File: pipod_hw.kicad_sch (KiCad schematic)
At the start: 0 parts

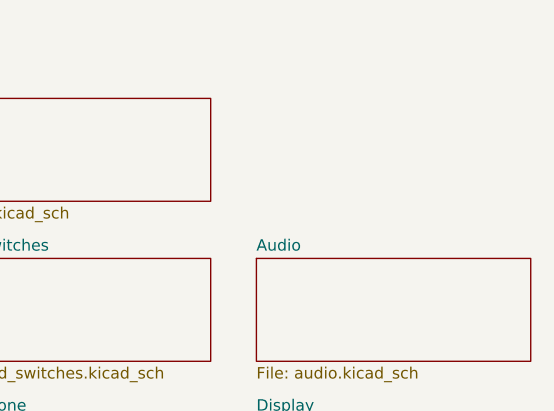
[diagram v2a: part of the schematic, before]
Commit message: integration: add mounting holes and connectors and second board
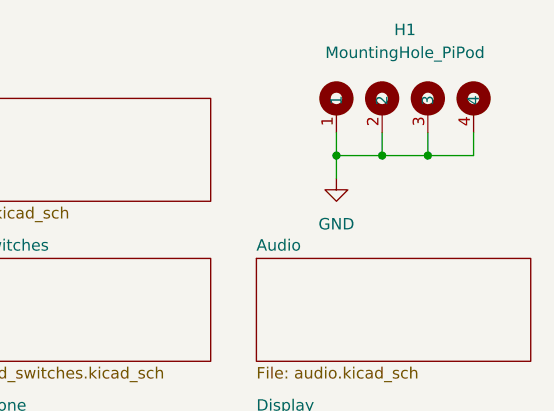
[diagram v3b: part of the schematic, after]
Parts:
- added H1: MountingHole_PiPod, pipod_hw:MountingHole_PiPod, symbol pipod_hw:MountingHole_PiPod
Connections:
- new net GND: H1.1, H1.2, H1.3, H1.4
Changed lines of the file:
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@@
 (kicad_sch (version 20211123) (generator eeschema)
   (paper "A4")
+  (junction (at 243.84 67.31) (diameter 0) (color 0 0 0 0)
+  )
+  (junction (at 233.68 67.31) (diameter 0) (color 0 0 0 0)
+  )
+  (junction (at 238.76 67.31) (diameter 0) (color 0 0 0 0)
+  )
+  (wire (pts (xy 238.76 67.31) (xy 233.68 67.31))
+    (stroke (width 0) (type default) (color 0 0 0 0))
+  )
+  (wire (pts (xy 233.68 64.77) (xy 233.68 67.31))
+    (stroke (width 0) (type default) (color 0 0 0 0))
+  )
+  (wire (pts (xy 248.92 64.77) (xy 248.92 67.31))
+    (stroke (width 0) (type default) (color 0 0 0 0))
+  )
+  (wire (pts (xy 243.84 64.77) (xy 243.84 67.31))
+    (stroke (width 0) (type default) (color 0 0 0 0))
+  )
+  (wire (pts (xy 243.84 67.31) (xy 238.76 67.31))
+    (stroke (width 0) (type default) (color 0 0 0 0))
+  )
+  (wire (pts (xy 233.68 67.31) (xy 233.68 69.85))
+    (stroke (width 0) (type default) (color 0 0 0 0))
+  )
+  (wire (pts (xy 248.92 67.31) (xy 243.84 67.31))
+    (stroke (width 0) (type default) (color 0 0 0 0))
+  )
+  (wire (pts (xy 238.76 64.77) (xy 238.76 67.31))
+    (stroke (width 0) (type default) (color 0 0 0 0))
+  )
+  (symbol (lib_id "pipod_hw:MountingHole_PiPod") (at 241.3 57.15 0) (unit 1)
+    (in_bom yes) (on_board yes) (fields_autoplaced)
+    (property "Reference" "H1" (id 0) (at 241.3 53.34 0))
+    (property "Value" "MountingHole_PiPod" (id 1) (at 241.3 55.88 0))
+    (property "Footprint" "pipod_hw:MountingHole_PiPod" (id 2) (at 241.3 57.15 0)
+      (effects (font (size 1.27 1.27)) hide)
+    )
+    (property "Datasheet" "" (id 3) (at 241.3 57.15 0)
+      (effects (font (size 1.27 1.27)) hide)
+    )
+    (pin "1")
+    (pin "2")
+    (pin "3")
+    (pin "4")
+  )
+  (symbol (lib_id "power:GND") (at 233.68 69.85 0) (unit 1)
+    (in_bom yes) (on_board yes) (fields_autoplaced)
+    (property "Reference" "#PWR0128" (id 0) (at 233.68 76.2 0)
+      (effects (font (size 1.27 1.27)) hide)
+    )
+    (property "Value" "GND" (id 1) (at 233.68 74.93 0))
+    (property "Footprint" "" (id 2) (at 233.68 69.85 0)
+      (effects (font (size 1.27 1.27)) hide)
+    )
+    (property "Datasheet" "" (id 3) (at 233.68 69.85 0)
+      (effects (font (size 1.27 1.27)) hide)
+    )
+    (pin "1")
+  )
   (sheet (at 189.23 78.74) (size 30.48 11.43) (fields_autoplaced)
     (stroke (width 0.1524) (type solid) (color 0 0 0 0))
@@
       (reference "#PWR0110") (unit 1) (value "GND") (footprint "")
     )
-    (path "/b0bb8e22-3ad5-4c36-b10d-7d4a51e22334/5f1a81a0-71fa-4e3a-b666-a1214c182b88"
+    (path "/b0bb8e22-3ad5-4c36-b10d-7d4a51e22334/c5850e11-500c-4afe-a940-57198437c49b"
       (reference "#PWR0111") (unit 1) (value "GND") (footprint "")
     )
@@
       (reference "#PWR0112") (unit 1) (value "GND") (footprint "")
     )
-    (path "/b0bb8e22-3ad5-4c36-b10d-7d4a51e22334/c9a079a4-a909-4c56-8f16-71ef57f1a02b"
+    (path "/b0bb8e22-3ad5-4c36-b10d-7d4a51e22334/92d3ff33-a56f-47b9-a155-1bb3f2f205ba"
       (reference "#PWR0113") (unit 1) (value "GND") (footprint "")
     )
-    (path "/b0bb8e22-3ad5-4c36-b10d-7d4a51e22334/7c31225e-d0aa-4e44-9f35-ab169480b0ab"
+    (path "/b0bb8e22-3ad5-4c36-b10d-7d4a51e22334/cc6524eb-94f3-4dfa-bdaa-99b0ca25d5ec"
       (reference "#PWR0114") (unit 1) (value "GND") (footprint "")
-    )
-    (path "/b0bb8e22-3ad5-4c36-b10d-7d4a51e22334/75ae250c-0f71-4135-b694-211ea9e1b346"
-      (reference "#PWR0115") (unit 1) (value "GND") (footprint "")
-    )
-    (path "/b0bb8e22-3ad5-4c36-b10d-7d4a51e22334/3afe4e73-fffb-46f1-9e1b-36443c4e46f7"
-      (reference "#PWR0116") (unit 1) (value "GND") (footprint "")
-    )
-    (path "/b0bb8e22-3ad5-4c36-b10d-7d4a51e22334/03da5625-23ea-48a9-8d0e-93afc8231c75"
-      (reference "#PWR0117") (unit 1) (value "GND") (footprint "")
-    )
-    (path "/b0bb8e22-3ad5-4c36-b10d-7d4a51e22334/c7b7372b-e3fe-413d-9bae-152c09962a64"
-      (reference "#PWR0118") (unit 1) (value "GND") (footprint "")
     )
     (path "/b0bb8e22-3ad5-4c36-b10d-7d4a51e22334/1187d984-3ec5-4c88-9c0f-ce193ae40d3e"
@@
       (reference "#PWR0127") (unit 1) (value "GNDA") (footprint "")
     )
+    (path "/c269cfd8-5b8f-4de0-b20e-7c84acf71936"
+      (reference "#PWR0128") (unit 1) (value "GND") (footprint "")
+    )
     (path "/9641055c-ce4b-4f2f-881f-d2622ca62ef8/69434326-4e70-4b27-bc99-d48bcdec69df"
       (reference "C1") (unit 1) (value "100n") (footprint "Capacitor_SMD:C_0402_1005Metric")
@@
       (reference "C53") (unit 1) (value "10u") (footprint "Capacitor_SMD:C_0402_1005Metric")
     )
-    (path "/b0bb8e22-3ad5-4c36-b10d-7d4a51e22334/dc70e79b-aa01-498d-83ce-04f8beba6a37"
-      (reference "CN1") (unit 1) (value "539160208") (footprint "lcsc:CONN-SMD_539160208")
-    )
-    (path "/b0bb8e22-3ad5-4c36-b10d-7d4a51e22334/d0e61b23-0984-4efd-a60c-569879ae3557"
-      (reference "CN2") (unit 1) (value "539160208") (footprint "lcsc:CONN-SMD_539160208")
-    )
     (path "/9641055c-ce4b-4f2f-881f-d2622ca62ef8/11a9f816-3064-4feb-beef-6cd42a49141b"
       (reference "D1") (unit 1) (value "MBRS130LT3G") (footprint "lcsc:SMB_L4.6-W3.6-LS5.3-RD")
@@
       (reference "DISP1") (unit 1) (value "STP240320_0200B") (footprint "Connector_Molex:Molex_SlimStack_54722-0164_2x08_P0.50mm_Vertical")
     )
+    (path "/b0bb8e22-3ad5-4c36-b10d-7d4a51e22334/3011643e-d10a-4918-abfd-3d280f17eb2f"
+      (reference "FPC1") (unit 1) (value "527462033") (footprint "lcsc:FPC-SMD_527462033")
+    )
+    (path "/b0bb8e22-3ad5-4c36-b10d-7d4a51e22334/3e4fc367-8c2e-4085-a0b0-e86f20d2a052"
+      (reference "FPC2") (unit 1) (value "527462033") (footprint "lcsc:FPC-SMD_527462033")
+    )
+    (path "/3a54314d-f300-4b26-9d74-86b079b327e3"
+      (reference "H1") (unit 1) (value "MountingHole_PiPod") (footprint "pipod_hw:MountingHole_PiPod")
+    )
     (path "/9641055c-ce4b-4f2f-881f-d2622ca62ef8/17c02880-df6f-4797-b976-af8c3295fb23"
       (reference "J3") (unit 1) (value "Conn_01x03_Male") (footprint "Gigahawk:Molex_PicoBlade_53047-0310_1x03_P1.25mm_Vertical")
@@
     )
     (path "/eadbe3e2-ad3f-4ca7-9baa-62c6cdfbb2dc/da0dae29-42d4-483a-9ab1-6e5fb7494f0a"
-      (reference "R12") (unit 1) (value "DNI") (footprint "")
+      (reference "R12") (unit 1) (value "DNI") (footprint "Resistor_SMD:R_0402_1005Metric")
     )
     (path "/f4aab422-c542-43e3-8476-eae6a2df1847/0a3de141-38e2-4729-972e-41552c2c892a"
@@
     )
     (path "/eadbe3e2-ad3f-4ca7-9baa-62c6cdfbb2dc/4a93418f-8918-4c8a-be3e-8ac6664b68e9"
-      (reference "R53") (unit 1) (value "10k") (footprint "")
+      (reference "R53") (unit 1) (value "10k") (footprint "Resistor_SMD:R_0402_1005Metric")
     )
     (path "/f4aab422-c542-43e3-8476-eae6a2df1847/dc354bb6-7b51-4421-92e0-ea2af5ff7fbb"

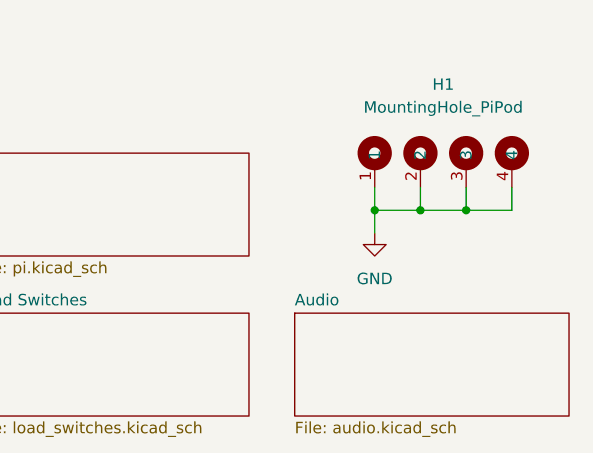
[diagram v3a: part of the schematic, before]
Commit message: schem: migrate away from LCSC exclusive parts
- layout: migrate away from lcsc footprints
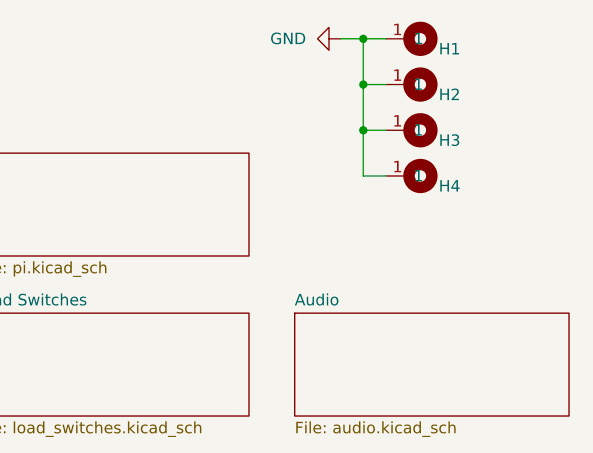
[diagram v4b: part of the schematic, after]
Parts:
- removed H1: MountingHole_PiPod, pipod_hw:MountingHole_PiPod, symbol pipod_hw:MountingHole_PiPod
- added H1, H2, H3, H4: (no value), symbol gigahawk:9774040243R
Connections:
- net GND: now also H1.1, H2.1, H3.1, H4.1

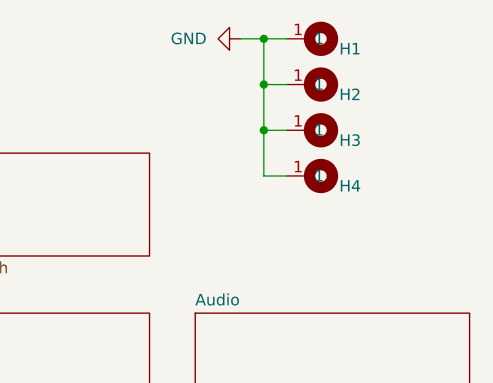
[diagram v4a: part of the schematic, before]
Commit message: layout: update footprint for TP4056M
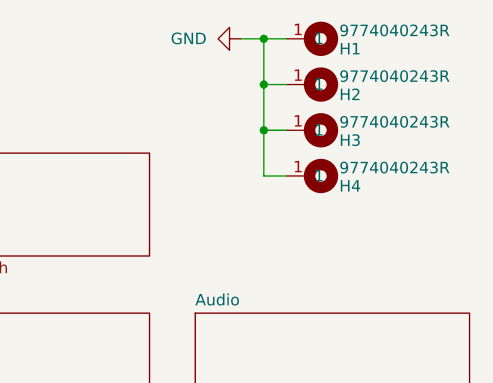
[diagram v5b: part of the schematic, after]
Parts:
- H1, H2, H3, H4: value (none) -> 9774040243R; footprint (none) -> Gigahawk:9774040243R
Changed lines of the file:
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@@
       (effects (font (size 1.27 1.27)) (justify left))
     )
-    (property "Value" "" (id 1) (at 240.792 47.371 90)
+    (property "Value" "9774040243R" (id 1) (at 240.792 47.371 90)
       (effects (font (size 1.27 1.27)) (justify left))
     )
-    (property "Footprint" "" (id 2) (at 242.57 48.26 0)
+    (property "Footprint" "Gigahawk:9774040243R" (id 2) (at 242.57 48.26 0)
       (effects (font (size 1.27 1.27)) hide)
     )
@@
       (effects (font (size 1.27 1.27)) (justify left))
     )
-    (property "Value" "" (id 1) (at 240.792 62.611 90)
+    (property "Value" "9774040243R" (id 1) (at 240.792 62.611 90)
       (effects (font (size 1.27 1.27)) (justify left))
     )
-    (property "Footprint" "" (id 2) (at 242.57 63.5 0)
+    (property "Footprint" "Gigahawk:9774040243R" (id 2) (at 242.57 63.5 0)
       (effects (font (size 1.27 1.27)) hide)
     )
@@
       (effects (font (size 1.27 1.27)) (justify left))
     )
-    (property "Value" "" (id 1) (at 240.792 52.451 90)
+    (property "Value" "9774040243R" (id 1) (at 240.792 52.451 90)
       (effects (font (size 1.27 1.27)) (justify left))
     )
-    (property "Footprint" "" (id 2) (at 242.57 53.34 0)
+    (property "Footprint" "Gigahawk:9774040243R" (id 2) (at 242.57 53.34 0)
       (effects (font (size 1.27 1.27)) hide)
     )
@@
       (effects (font (size 1.27 1.27)) (justify left))
     )
-    (property "Value" "" (id 1) (at 240.792 57.531 90)
+    (property "Value" "9774040243R" (id 1) (at 240.792 57.531 90)
       (effects (font (size 1.27 1.27)) (justify left))
     )
-    (property "Footprint" "" (id 2) (at 242.57 58.42 0)
+    (property "Footprint" "Gigahawk:9774040243R" (id 2) (at 242.57 58.42 0)
       (effects (font (size 1.27 1.27)) hide)
     )
@@
     )
     (path "/9641055c-ce4b-4f2f-881f-d2622ca62ef8/6413ea7d-db9d-4aaf-8097-6256affe6826"
-      (reference "U2") (unit 1) (value "TP4056M") (footprint "Package_SO:MSOP-8-1EP_3x3mm_P0.65mm_EP1.95x2.15mm")
+      (reference "U2") (unit 1) (value "TP4056M") (footprint "Gigahawk:MSOP-8-1EP_3x3mm_P0.65mm_EP1.425x1.76mm")
     )
     (path "/9641055c-ce4b-4f2f-881f-d2622ca62ef8/2691c01f-307c-4fef-82f3-f9029f5d5c5a"

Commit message: layout, routing: relayout and reroute board
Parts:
- removed H3, H4: 9774040243R, Gigahawk:9774040243R, symbol gigahawk:9774040243R
- H1, H2: value 9774040243R -> (none); footprint Gigahawk:9774040243R -> (none)
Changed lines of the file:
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@@
   (junction (at 232.41 48.26) (diameter 0) (color 0 0 0 0)
-  )
-  (junction (at 232.41 58.42) (diameter 0) (color 0 0 0 0)
-  )
-  (junction (at 232.41 53.34) (diameter 0) (color 0 0 0 0)
-  )
-  (wire (pts (xy 232.41 63.5) (xy 232.41 58.42))
-    (stroke (width 0) (type default) (color 0 0 0 0))
   )
   (wire (pts (xy 232.41 53.34) (xy 232.41 48.26))
     (stroke (width 0) (type default) (color 0 0 0 0))
   )
-  (wire (pts (xy 232.41 58.42) (xy 232.41 53.34))
-    (stroke (width 0) (type default) (color 0 0 0 0))
-  )
   (wire (pts (xy 234.95 53.34) (xy 232.41 53.34))
     (stroke (width 0) (type default) (color 0 0 0 0))
   )
   (wire (pts (xy 229.87 48.26) (xy 232.41 48.26))
-    (stroke (width 0) (type default) (color 0 0 0 0))
-  )
-  (wire (pts (xy 234.95 63.5) (xy 232.41 63.5))
-    (stroke (width 0) (type default) (color 0 0 0 0))
-  )
-  (wire (pts (xy 234.95 58.42) (xy 232.41 58.42))
     (stroke (width 0) (type default) (color 0 0 0 0))
   )
@@
       (effects (font (size 1.27 1.27)) (justify left))
     )
-    (property "Value" "9774040243R" (id 1) (at 240.792 47.371 90)
+    (property "Value" "" (id 1) (at 240.792 47.371 90)
       (effects (font (size 1.27 1.27)) (justify left))
     )
-    (property "Footprint" "Gigahawk:9774040243R" (id 2) (at 242.57 48.26 0)
+    (property "Footprint" "" (id 2) (at 242.57 48.26 0)
       (effects (font (size 1.27 1.27)) hide)
     )
@@
     )
     (property "Description" "Round Standoff Threaded M2x0.4 Steel 0.157\" (4.00mm)" (id 12) (at 242.57 48.26 0)
-      (effects (font (size 1.27 1.27)) hide)
-    )
-    (pin "1")
-  )
-  (symbol (lib_id "gigahawk:9774040243R") (at 242.57 63.5 270) (unit 1)
-    (in_bom yes) (on_board yes)
-    (property "Reference" "H4" (id 0) (at 240.792 64.643 90)
-      (effects (font (size 1.27 1.27)) (justify left))
-    )
-    (property "Value" "9774040243R" (id 1) (at 240.792 62.611 90)
-      (effects (font (size 1.27 1.27)) (justify left))
-    )
-    (property "Footprint" "Gigahawk:9774040243R" (id 2) (at 242.57 63.5 0)
-      (effects (font (size 1.27 1.27)) hide)
-    )
-    (property "Datasheet" "https://media.digikey.com/pdf/Data%20Sheets/Wurth%20Electronics%20PDFs/WA-SMSx_Performance_Flyer.pdf" (id 3) (at 242.57 63.5 0)
-      (effects (font (size 1.27 1.27)) hide)
-    )
-    (property "Manufacturer Part" "9774040243R" (id 4) (at 242.57 63.5 0)
-      (effects (font (size 1.27 1.27)) hide)
-    )
-    (property "Digikey Part" "732-7090-2-ND" (id 5) (at 242.57 63.5 0)
-      (effects (font (size 1.27 1.27)) hide)
-    )
-    (property "Digikey Price/Stock" "https://www.digikey.com/en/products/detail/w%C3%BCrth-elektronik/9774040243R/5320633" (id 6) (at 242.57 63.5 0)
-      (effects (font (size 1.27 1.27)) hide)
-    )
-    (property "Manufacturer" "Würth Elektronik" (id 7) (at 242.57 63.5 0)
-      (effects (font (size 1.27 1.27)) hide)
-    )
-    (property "JLC Part" "" (id 8) (at 242.57 63.5 0)
-      (effects (font (size 1.27 1.27)) hide)
-    )
-    (property "LCSC Part" "" (id 9) (at 242.57 63.5 0)
-      (effects (font (size 1.27 1.27)) hide)
-    )
-    (property "Mouser Part" "710-9774040243R" (id 10) (at 242.57 63.5 0)
-      (effects (font (size 1.27 1.27)) hide)
-    )
-    (property "Mouser Price/Stock" "https://www.mouser.ca/ProductDetail/Wurth-Elektronik/9774040243R?qs=KRpiEsko4HmaEKFu8pgBnw%3D%3D" (id 11) (at 242.57 63.5 0)
-      (effects (font (size 1.27 1.27)) hide)
-    )
-    (property "Description" "Round Standoff Threaded M2x0.4 Steel 0.157\" (4.00mm)" (id 12) (at 242.57 63.5 0)
       (effects (font (size 1.27 1.27)) hide)
     )
@@
       (effects (font (size 1.27 1.27)) (justify left))
     )
-    (property "Value" "9774040243R" (id 1) (at 240.792 52.451 90)
+    (property "Value" "" (id 1) (at 240.792 52.451 90)
       (effects (font (size 1.27 1.27)) (justify left))
     )
-    (property "Footprint" "Gigahawk:9774040243R" (id 2) (at 242.57 53.34 0)
+    (property "Footprint" "" (id 2) (at 242.57 53.34 0)
       (effects (font (size 1.27 1.27)) hide)
     )
@@
     )
     (property "Description" "Round Standoff Threaded M2x0.4 Steel 0.157\" (4.00mm)" (id 12) (at 242.57 53.34 0)
-      (effects (font (size 1.27 1.27)) hide)
-    )
-    (pin "1")
-  )
-  (symbol (lib_id "gigahawk:9774040243R") (at 242.57 58.42 270) (unit 1)
-    (in_bom yes) (on_board yes)
-    (property "Reference" "H3" (id 0) (at 240.792 59.563 90)
-      (effects (font (size 1.27 1.27)) (justify left))
-    )
-    (property "Value" "9774040243R" (id 1) (at 240.792 57.531 90)
-      (effects (font (size 1.27 1.27)) (justify left))
-    )
-    (property "Footprint" "Gigahawk:9774040243R" (id 2) (at 242.57 58.42 0)
-      (effects (font (size 1.27 1.27)) hide)
-    )
-    (property "Datasheet" "https://media.digikey.com/pdf/Data%20Sheets/Wurth%20Electronics%20PDFs/WA-SMSx_Performance_Flyer.pdf" (id 3) (at 242.57 58.42 0)
-      (effects (font (size 1.27 1.27)) hide)
-    )
-    (property "Manufacturer Part" "9774040243R" (id 4) (at 242.57 58.42 0)
-      (effects (font (size 1.27 1.27)) hide)
-    )
-    (property "Digikey Part" "732-7090-2-ND" (id 5) (at 242.57 58.42 0)
-      (effects (font (size 1.27 1.27)) hide)
-    )
-    (property "Digikey Price/Stock" "https://www.digikey.com/en/products/detail/w%C3%BCrth-elektronik/9774040243R/5320633" (id 6) (at 242.57 58.42 0)
-      (effects (font (size 1.27 1.27)) hide)
-    )
-    (property "Manufacturer" "Würth Elektronik" (id 7) (at 242.57 58.42 0)
-      (effects (font (size 1.27 1.27)) hide)
-    )
-    (property "JLC Part" "" (id 8) (at 242.57 58.42 0)
-      (effects (font (size 1.27 1.27)) hide)
-    )
-    (property "LCSC Part" "" (id 9) (at 242.57 58.42 0)
-      (effects (font (size 1.27 1.27)) hide)
-    )
-    (property "Mouser Part" "710-9774040243R" (id 10) (at 242.57 58.42 0)
-      (effects (font (size 1.27 1.27)) hide)
-    )
-    (property "Mouser Price/Stock" "https://www.mouser.ca/ProductDetail/Wurth-Elektronik/9774040243R?qs=KRpiEsko4HmaEKFu8pgBnw%3D%3D" (id 11) (at 242.57 58.42 0)
-      (effects (font (size 1.27 1.27)) hide)
-    )
-    (property "Description" "Round Standoff Threaded M2x0.4 Steel 0.157\" (4.00mm)" (id 12) (at 242.57 58.42 0)
       (effects (font (size 1.27 1.27)) hide)
     )
@@
       (reference "#PWR057") (unit 1) (value "GND") (footprint "")
     )
+    (path "/f4aab422-c542-43e3-8476-eae6a2df1847/1be928ce-636d-4c5b-8bdc-3168d1df379d"
+      (reference "#PWR058") (unit 1) (value "+3.3V") (footprint "")
+    )
     (path "/8ab03be1-4611-483d-92bd-219df6757e0e/85ecf29f-26e8-4164-9205-869c23e1c595"
       (reference "#PWR059") (unit 1) (value "GND") (footprint "")
@@
       (reference "#PWR0129") (unit 1) (value "GND") (footprint "")
     )
+    (path "/f4aab422-c542-43e3-8476-eae6a2df1847/15753bae-56c4-4edb-850b-91055dca8a07"
+      (reference "#PWR0130") (unit 1) (value "+3.3V") (footprint "")
+    )
     (path "/b0bb8e22-3ad5-4c36-b10d-7d4a51e22334/1187d984-3ec5-4c88-9c0f-ce193ae40d3e"
       (reference "#PWR0132") (unit 1) (value "GND") (footprint "")
@@
       (reference "H2") (unit 1) (value "9774040243R") (footprint "Gigahawk:9774040243R")
     )
-    (path "/fca9c1b3-55b0-49cb-8bcd-7f7f26359ffc"
-      (reference "H3") (unit 1) (value "9774040243R") (footprint "Gigahawk:9774040243R")
-    )
-    (path "/ac457337-d739-4276-9ff8-18f2f37b30df"
-      (reference "H4") (unit 1) (value "9774040243R") (footprint "Gigahawk:9774040243R")
-    )
     (path "/9641055c-ce4b-4f2f-881f-d2622ca62ef8/17c02880-df6f-4797-b976-af8c3295fb23"
       (reference "J1") (unit 1) (value "Conn_01x03_Male") (footprint "Gigahawk:Molex_PicoBlade_53047-0310_1x03_P1.25mm_Vertical")
@@
       (reference "R45") (unit 1) (value "10k") (footprint "Resistor_SMD:R_0402_1005Metric")
     )
+    (path "/f4aab422-c542-43e3-8476-eae6a2df1847/67c16967-8f9e-4fee-8ae7-719d7fb93e22"
+      (reference "R46") (unit 1) (value "10k") (footprint "Resistor_SMD:R_0402_1005Metric")
+    )
+    (path "/f4aab422-c542-43e3-8476-eae6a2df1847/985c1764-9529-4a96-b11d-300a6781bacf"
+      (reference "R47") (unit 1) (value "10k") (footprint "Resistor_SMD:R_0402_1005Metric")
+    )
     (path "/f4aab422-c542-43e3-8476-eae6a2df1847/dc354bb6-7b51-4421-92e0-ea2af5ff7fbb"
       (reference "TP1") (unit 1) (value "TestPoint") (footprint "TestPoint:TestPoint_Pad_D1.5mm")
@@
     )
     (path "/f4aab422-c542-43e3-8476-eae6a2df1847/a1cd96cb-1cf2-42af-8049-9350ef4d78e3"
-      (reference "U5") (unit 1) (value "W25Q128JVS") (footprint "Package_SO:SOIC-8_5.23x5.23mm_P1.27mm")
+      (reference "U5") (unit 1) (value "W25Q128JVS") (footprint "Package_SON:WSON-8-1EP_6x5mm_P1.27mm_EP3.4x4.3mm")
     )
     (path "/f4aab422-c542-43e3-8476-eae6a2df1847/ec102973-8c1e-44ac-b5ab-fa9e9ce69d0a"
@@
     )
     (path "/f4aab422-c542-43e3-8476-eae6a2df1847/a57c84b5-5d55-414c-b5d7-cf18bbcbc814"
-      (reference "Y1") (unit 1) (value "12MHz 20pF") (footprint "Crystal:Crystal_SMD_3225-4Pin_3.2x2.5mm")
-    )
-  )
+      (reference "Y1") (unit 1) (value "12MHz 20pF") (footprint "Crystal:Crystal_SMD_2520-4Pin_2.5x2.0mm")
+    )
+  )
